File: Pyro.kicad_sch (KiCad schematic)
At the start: 3 parts

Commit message: Rev 4 issued for production
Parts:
- removed D5: (no value), symbol Diode:1N914
- removed Q1: (no value), symbol Device:Q_NMOS_GDS
- removed RN2: (no value), Resistor_SMD:R_Array_Convex_4x0603, symbol Device:R_Pack04_Split
- added D2: B5819W SL, Diode_SMD:D_SOD-123, symbol Diode:1N914
- added Q1: AO3400A, Package_TO_SOT_SMD:SOT-23, symbol Transistor_FET:AO3400A
- added R5: 5, Resistor_SMD:R_0805_2012Metric, symbol Device:R
- added RN1: 10k, Resistor_SMD:R_Array_Convex_4x0603, symbol Device:R_Pack04_Split
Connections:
- net +3V3: now also D2.1 (K)
- net Cont: now also D2.2 (A), Q1.2 (S), RN1.2 (R2.1), RN1.6 (R3.2)
- net GND: now also RN1.1 (R1.1), RN1.4 (R4.1)
- net Pyro: now also Q1.1 (G), RN1.8 (R1.2)
- new net: Q1.3 (D), R5.2
- new net: RN1.3 (R3.1), RN1.5 (R4.2)
- new net ARM: R5.1, RN1.7 (R2.2)
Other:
- note added: "1/2 ohms"
- title: (none) -> Pyro Channel

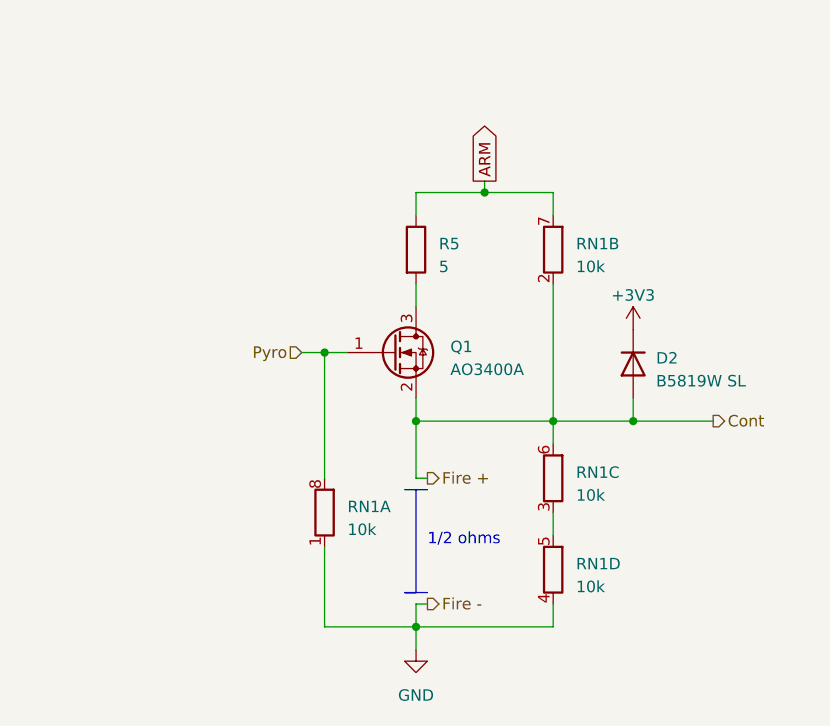
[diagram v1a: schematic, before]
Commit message: Add current limit resistor between pyro channel and pin.
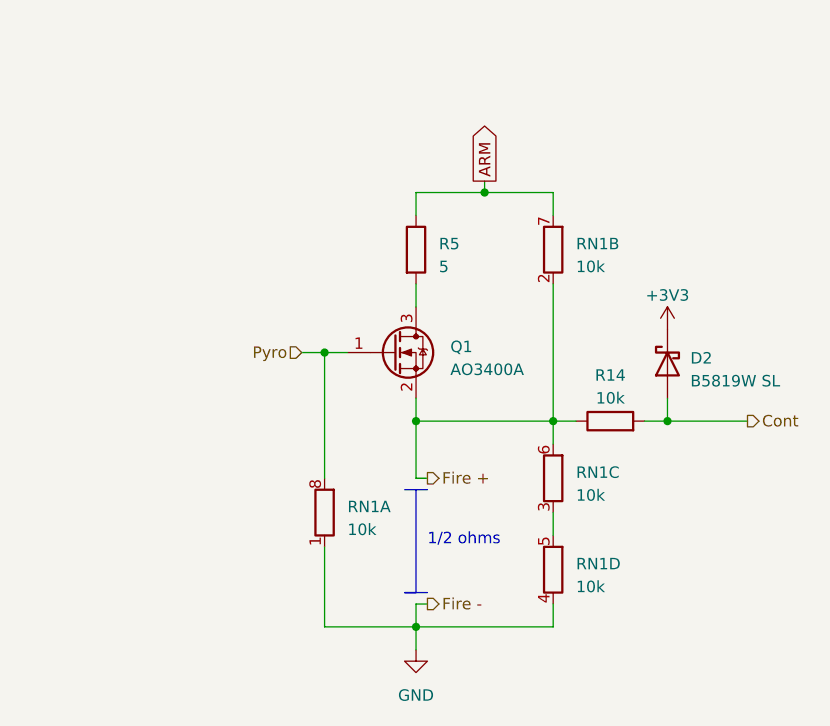
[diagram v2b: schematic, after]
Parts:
- added R14: 10k, Resistor_SMD:R_0603_1608Metric, symbol Device:R
- D2: symbol Diode:1N914 -> Diode:1N5822
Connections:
- net Cont: now also R14.2; no longer Q1.2 (S), RN1.2 (R2.1), RN1.6 (R3.2)
- new net Fire +: Q1.2 (S), R14.1, RN1.2 (R2.1), RN1.6 (R3.2)
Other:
- moved on the sheet: D2
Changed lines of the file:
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@@
   (junction (at 139.7 54.61) (diameter 0) (color 0 0 0 0)
   )
-  (junction (at 156.21 80.01) (diameter 0) (color 0 0 0 0)
-  )
   (junction (at 147.32 80.01) (diameter 0) (color 0 0 0 0)
   )
+  (junction (at 160.02 80.01) (diameter 0) (color 0 0 0 0)
+  )
   (junction (at 121.92 72.39) (diameter 0) (color 0 0 0 0)
   )
@@
     (stroke (width 0) (type default))
   )
-  (wire (pts (xy 156.21 80.01) (xy 165.1 80.01))
+  (wire (pts (xy 160.02 80.01) (xy 168.91 80.01))
+    (stroke (width 0) (type default))
+  )
+  (wire (pts (xy 147.32 80.01) (xy 149.86 80.01))
     (stroke (width 0) (type default))
   )
@@
     (stroke (width 0) (type default))
   )
-  (wire (pts (xy 147.32 80.01) (xy 156.21 80.01))
-    (stroke (width 0) (type default))
-  )
   (wire (pts (xy 132.08 100.33) (xy 133.35 100.33))
     (stroke (width 0) (type default))
   )
+  (wire (pts (xy 157.48 80.01) (xy 160.02 80.01))
+    (stroke (width 0) (type default))
+  )
   (wire (pts (xy 133.35 86.36) (xy 132.08 86.36))
     (stroke (width 0) (type default))
@@
     (stroke (width 0) (type default))
   )
-  (wire (pts (xy 156.21 77.47) (xy 156.21 80.01))
+  (wire (pts (xy 160.02 77.47) (xy 160.02 80.01))
     (stroke (width 0) (type default))
   )
@@
     (effects (font (size 1.27 1.27)) (justify left))
   )
-  (hierarchical_label "Cont" (shape output) (at 165.1 80.01 0) (fields_autoplaced)
+  (hierarchical_label "Cont" (shape output) (at 168.91 80.01 0) (fields_autoplaced)
     (effects (font (size 1.27 1.27)) (justify left))
   )
@@
   (hierarchical_label "Fire +" (shape output) (at 133.35 86.36 0) (fields_autoplaced)
     (effects (font (size 1.27 1.27)) (justify left))
+  )
+  (symbol (lib_id "Device:R") (at 153.67 80.01 90) (unit 1)
+    (in_bom yes) (on_board yes) (dnp no) (fields_autoplaced)
+    (property "Reference" "R14" (at 153.67 74.93 90)
+      (effects (font (size 1.27 1.27)))
+    )
+    (property "Value" "10k" (at 153.67 77.47 90)
+      (effects (font (size 1.27 1.27)))
+    )
+    (property "Footprint" "Resistor_SMD:R_0603_1608Metric" (at 153.67 81.788 90)
+      (effects (font (size 1.27 1.27)) hide)
+    )
+    (property "Datasheet" "~" (at 153.67 80.01 0)
+      (effects (font (size 1.27 1.27)) hide)
+    )
+    (property "LCSC" "C247080" (at 153.67 80.01 0)
+      (effects (font (size 1.27 1.27)) hide)
+    )
+    (property "JLC" "0805" (at 153.67 80.01 0)
+      (effects (font (size 1.27 1.27)) hide)
+    )
+    (pin "1")
+    (pin "2")
+    (instances
+      (project "bob"
+        (path "/febb7d9c-f8af-428a-b455-1415daa5c3f8/fd9f7e93-7f62-4ad6-9840-ded72998171a"
+          (reference "R14") (unit 1)
+        )
+        (path "/febb7d9c-f8af-428a-b455-1415daa5c3f8/08429985-15e5-45d8-bdd5-5d10e1876be4"
+          (reference "R15") (unit 1)
+        )
+      )
+    )
   )
   (symbol (lib_id "Device:R_Pack04_Split") (at 147.32 60.96 0) (unit 2)
@@
     )
   )
-  (symbol (lib_id "Diode:1N914") (at 156.21 73.66 90) (mirror x) (unit 1)
-    (in_bom yes) (on_board yes) (dnp no) (fields_autoplaced)
-    (property "Reference" "D2" (at 158.75 73.025 90)
+  (symbol (lib_id "Diode:1N5822") (at 160.02 73.66 90) (mirror x) (unit 1)
+    (in_bom yes) (on_board yes) (dnp no) (fields_autoplaced)
+    (property "Reference" "D2" (at 162.56 73.025 90)
       (effects (font (size 1.27 1.27)) (justify right))
     )
-    (property "Value" "B5819W SL" (at 158.75 75.565 90)
+    (property "Value" "B5819W SL" (at 162.56 75.565 90)
       (effects (font (size 1.27 1.27)) (justify right))
     )
-    (property "Footprint" "Diode_SMD:D_SOD-123" (at 160.655 73.66 0)
-      (effects (font (size 1.27 1.27)) hide)
-    )
-    (property "Datasheet" "https://jlcpcb.com/b454aea9-40e7-422f-bffa-9f112dad248c" (at 156.21 73.66 0)
-      (effects (font (size 1.27 1.27)) hide)
-    )
-    (property "LCSC" "C8598" (at 156.21 73.66 0)
-      (effects (font (size 1.27 1.27)) hide)
-    )
-    (property "JLC" "SOD-123FL" (at 156.21 73.66 0)
+    (property "Footprint" "Diode_SMD:D_SOD-123" (at 164.465 73.66 0)
+      (effects (font (size 1.27 1.27)) hide)
+    )
+    (property "Datasheet" "http://www.vishay.com/docs/88526/1n5820.pdf" (at 160.02 73.66 0)
+      (effects (font (size 1.27 1.27)) hide)
+    )
+    (property "LCSC" "C8598" (at 160.02 73.66 0)
+      (effects (font (size 1.27 1.27)) hide)
+    )
+    (property "JLC" "SOD-123FL" (at 160.02 73.66 0)
       (effects (font (size 1.27 1.27)) hide)
     )
@@
     )
   )
-  (symbol (lib_id "power:+3V3") (at 156.21 69.85 0) (unit 1)
-    (in_bom yes) (on_board yes) (dnp no) (fields_autoplaced)
-    (property "Reference" "#PWR055" (at 156.21 73.66 0)
-      (effects (font (size 1.27 1.27)) hide)
-    )
-    (property "Value" "+3V3" (at 156.21 66.04 0)
+  (symbol (lib_id "power:+3V3") (at 160.02 69.85 0) (unit 1)
+    (in_bom yes) (on_board yes) (dnp no) (fields_autoplaced)
+    (property "Reference" "#PWR055" (at 160.02 73.66 0)
+      (effects (font (size 1.27 1.27)) hide)
+    )
+    (property "Value" "+3V3" (at 160.02 66.04 0)
       (effects (font (size 1.27 1.27)))
     )
-    (property "Footprint" "" (at 156.21 69.85 0)
-      (effects (font (size 1.27 1.27)) hide)
-    )
-    (property "Datasheet" "" (at 156.21 69.85 0)
-      (effects (font (size 1.27 1.27)) hide)
-    )
+    (property "Footprint" "" (at 160.02 69.85 0)
+      (effects (font (size 1.27 1.27)) hide)
+    )
+    (property "Datasheet" "" (at 160.02 69.85 0)
+      (effects (font (size 1.27 1.27)) hide)
+    )
